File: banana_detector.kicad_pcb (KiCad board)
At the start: 2 copper layers, 70 x 30 mm, 49 parts, among them J1 supply, J2 NRST_button, J3 USER_button, J4 Conn_01x04_Pin, J5 Conn_01x04_Pin, J6 Conn_01x02_Pin, Q1 BSS123, U1 AMS1117, U2 STM32G030F6Px, U3 TL082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

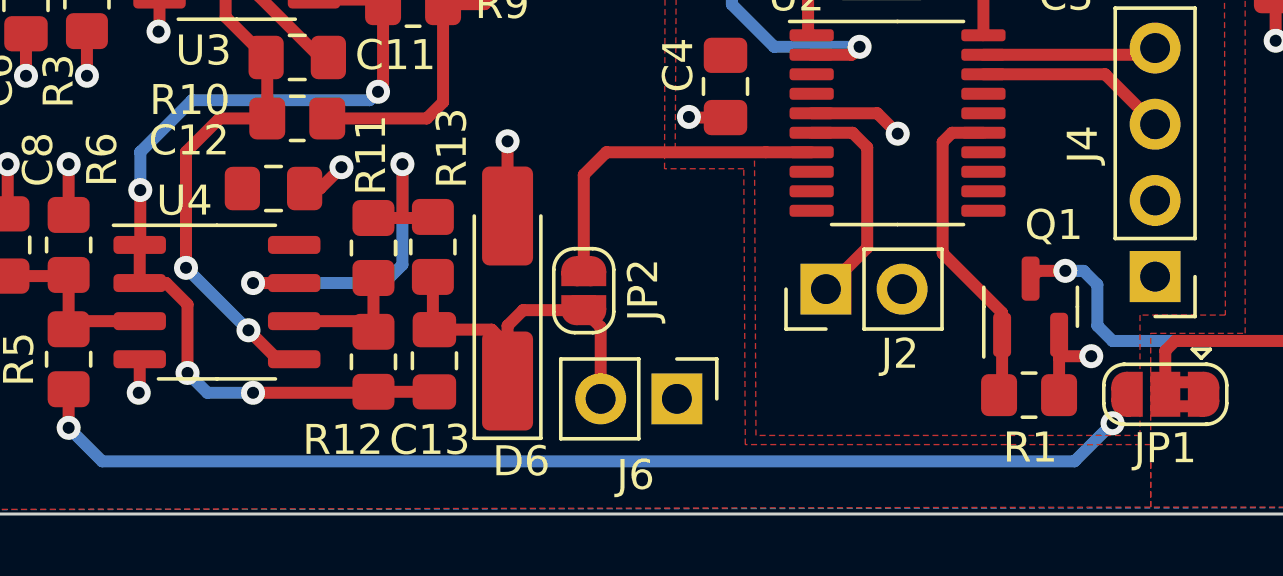
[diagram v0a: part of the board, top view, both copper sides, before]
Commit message: op amp type update, lm358->tl082, bulk purchase=cheaper, higher badwidth, still super cheap
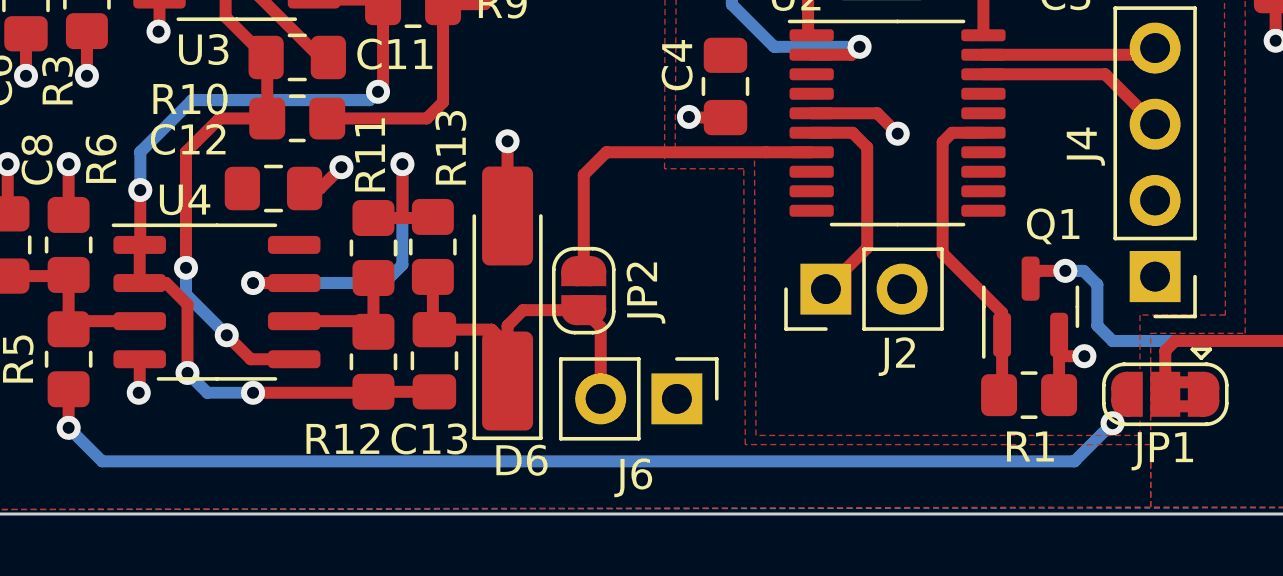
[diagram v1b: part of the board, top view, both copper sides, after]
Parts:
- U4: value LM358 -> TL082
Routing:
- net Net-(U4B-+): track 21.5 -> 22.1 mm
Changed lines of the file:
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@@
         (effects (font (size 1 1) (thickness 0.15)))
     )
-    (fp_text value "LM358" (at 0 3.4) (layer "F.Fab")
+    (fp_text value "TL082" (at 0 3.4) (layer "F.Fab")
         (effects (font (size 1 1) (thickness 0.15)))
     )
@@
   (segment (start 131.6228 118.618) (end 131.6228 120.3104) (width 0.4) (layer "F.Cu") (net 2))
   (segment (start 140.0048 119.4308) (end 140.716 118.7196) (width 0.4) (layer "F.Cu") (net 2))
-  (segment (start 165.7096 125.0188) (end 164.6886 125.0188) (width 0.4) (layer "F.Cu") (net 2))
   (segment (start 146.2532 120.3452) (end 146.2532 117.856) (width 0.4) (layer "F.Cu") (net 2))
+  (segment (start 164.6886 125.0188) (end 164.6378 125.0696) (width 0.4) (layer "F.Cu") (net 2))
   (segment (start 138.1252 107.0864) (end 138.1252 105.664) (width 0.4) (layer "F.Cu") (net 2))
   (segment (start 166.9656 108.7632) (end 165.2528 108.7632) (width 0.4) (layer "F.Cu") (net 2))
@@
   (segment (start 171.8564 113.0007) (end 171.8564 114.5032) (width 0.4) (layer "F.Cu") (net 2))
   (segment (start 133.9912 125.1204) (end 133.9912 126.2064) (width 0.4) (layer "F.Cu") (net 2))
+  (segment (start 165.481 125.0188) (end 164.6886 125.0188) (width 0.4) (layer "F.Cu") (net 2))
   (segment (start 134.6516 113.1316) (end 134.6516 114.1668) (width 0.4) (layer "F.Cu") (net 2))
   (segment (start 129.5908 120.2729) (end 129.5908 118.618) (width 0.4) (layer "F.Cu") (net 2))
   (segment (start 133.9912 126.2064) (end 133.9596 126.238) (width 0.4) (layer "F.Cu") (net 2))
-  (segment (start 164.6886 125.0188) (end 164.6378 125.0696) (width 0.4) (layer "F.Cu") (net 2))
   (segment (start 164.6378 124.3076) (end 164.6378 125.0696) (width 0.4) (layer "F.Cu") (net 2))
   (segment (start 139.489 119.4308) (end 140.0048 119.4308) (width 0.4) (layer "F.Cu") (net 2))
@@
   (via (at 140.716 118.7196) (size 0.8) (drill 0.4) (layers "F.Cu" "B.Cu") (net 2))
   (via (at 164.7952 111.6076) (size 0.8) (drill 0.4) (layers "F.Cu" "B.Cu") (net 2))
-  (via (at 165.7096 125.0188) (size 0.8) (drill 0.4) (layers "F.Cu" "B.Cu") (net 2))
+  (via (at 165.481 125.0188) (size 0.8) (drill 0.4) (layers "F.Cu" "B.Cu") (net 2))
   (via (at 134.62 114.1984) (size 0.8) (drill 0.4) (layers "F.Cu" "B.Cu") (net 2))
   (via (at 133.9596 126.238) (size 0.8) (drill 0.4) (layers "F.Cu" "B.Cu") (net 2))
@@
   (segment (start 139.8016 111.8616) (end 142.1732 111.8616) (width 0.4) (layer "F.Cu") (net 9))
   (segment (start 140.007749 115.062) (end 140.2803 115.062) (width 0.4) (layer "F.Cu") (net 9))
+  (segment (start 136.8933 124.3203) (end 137.6934 125.1204) (width 0.4) (layer "F.Cu") (net 10))
   (segment (start 136.8552 113.7119) (end 136.8552 111.252) (width 0.4) (layer "F.Cu") (net 10))
   (segment (start 138.2428 117.094) (end 138.2428 115.0995) (width 0.4) (layer "F.Cu") (net 10))
@@
   (segment (start 137.5156 110.5916) (end 139.8016 110.5916) (width 0.4) (layer "F.Cu") (net 10))
   (segment (start 138.2428 115.0995) (end 138.2053 115.062) (width 0.4) (layer "F.Cu") (net 10))
-  (segment (start 137.6172 124.1552) (end 138.5824 125.1204) (width 0.4) (layer "F.Cu") (net 10))
   (segment (start 135.5344 122.0724) (end 135.5344 118.2116) (width 0.4) (layer "F.Cu") (net 10))
   (segment (start 138.2053 115.062) (end 136.8552 113.7119) (width 0.4) (layer "F.Cu") (net 10))
+  (segment (start 137.6934 125.1204) (end 139.1412 125.1204) (width 0.4) (layer "F.Cu") (net 10))
   (segment (start 135.5344 118.2116) (end 136.652 117.094) (width 0.4) (layer "F.Cu") (net 10))
-  (segment (start 138.5824 125.1204) (end 139.1412 125.1204) (width 0.4) (layer "F.Cu") (net 10))
   (segment (start 136.8552 111.252) (end 137.5156 110.5916) (width 0.4) (layer "F.Cu") (net 10))
-  (via (at 137.6172 124.1552) (size 0.8) (drill 0.4) (layers "F.Cu" "B.Cu") (net 10))
+  (via (at 136.8933 124.3203) (size 0.8) (drill 0.4) (layers "F.Cu" "B.Cu") (net 10))
   (via (at 135.5344 122.0724) (size 0.8) (drill 0.4) (layers "F.Cu" "B.Cu") (net 10))
-  (segment (start 137.6172 124.1552) (end 135.5344 122.0724) (width 0.4) (layer "B.Cu") (net 10))
+  (segment (start 136.8933 124.3203) (end 135.5344 122.9614) (width 0.4) (layer "B.Cu") (net 10))
+  (segment (start 135.5344 122.9614) (end 135.5344 122.0724) (width 0.4) (layer "B.Cu") (net 10))
   (segment (start 149.357 126.4412) (end 149.357 124.0482) (width 0.4) (layer "F.Cu") (net 11))
   (segment (start 148.7932 123.4844) (end 146.7716 123.4844) (width 0.4) (layer "F.Cu") (net 11))
@@
   (segment (start 139.8016 113.1316) (end 141.9512 113.1316) (width 0.4) (layer "F.Cu") (net 12))
   (segment (start 141.9352 116.205) (end 142.1036 116.0366) (width 0.4) (layer "F.Cu") (net 12))
+  (segment (start 137.7696 126.238) (end 141.7508 126.238) (width 0.4) (layer "F.Cu") (net 12))
   (segment (start 134.0104 121.2912) (end 133.9912 121.3104) (width 0.4) (layer "F.Cu") (net 12))
   (segment (start 142.1036 116.0366) (end 142.1036 113.284) (width 0.4) (layer "F.Cu") (net 12))
@@
   (segment (start 134.0104 119.4816) (end 134.0104 121.2912) (width 0.4) (layer "F.Cu") (net 12))
   (segment (start 135.5852 125.5776) (end 135.5852 123.2916) (width 0.4) (layer "F.Cu") (net 12))
-  (segment (start 137.7696 126.238) (end 141.7508 126.238) (width 0.4) (layer "F.Cu") (net 12))
   (via (at 134.0104 119.4816) (size 0.8) (drill 0.4) (layers "F.Cu" "B.Cu") (net 12))
   (via (at 135.5852 125.5776) (size 0.8) (drill 0.4) (layers "F.Cu" "B.Cu") (net 12))
